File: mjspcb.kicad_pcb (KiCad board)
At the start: 2 copper layers, 83.3 x 40.1 mm, 78 parts, among them P1 Batteries, P10 Lipo, P2 serial breakout, P3 I2C breakout, P4 GPS, P5 piezo, P6 BPW34, P7 electrodes, P8 perfboard breakout, P9 reset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

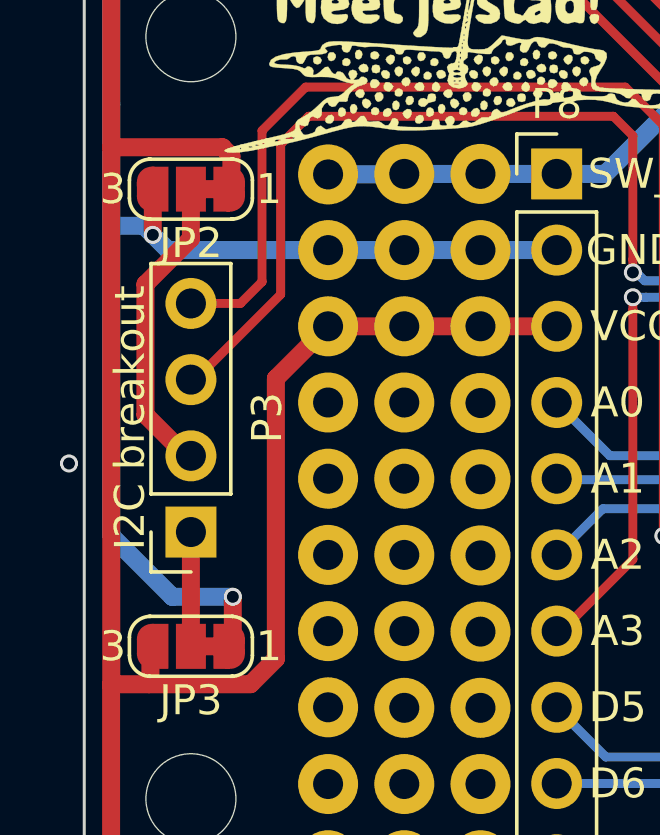
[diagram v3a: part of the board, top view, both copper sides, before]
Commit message: Fix DRC errors in solder jumper footprint
This uses a modified solder jumper footprint that has a graphic polygon
rather than overlapping pads to connect the default pins, which prevents
DRC errors. See: https://github.com/KiCad/kicad-footprints/issues/1165
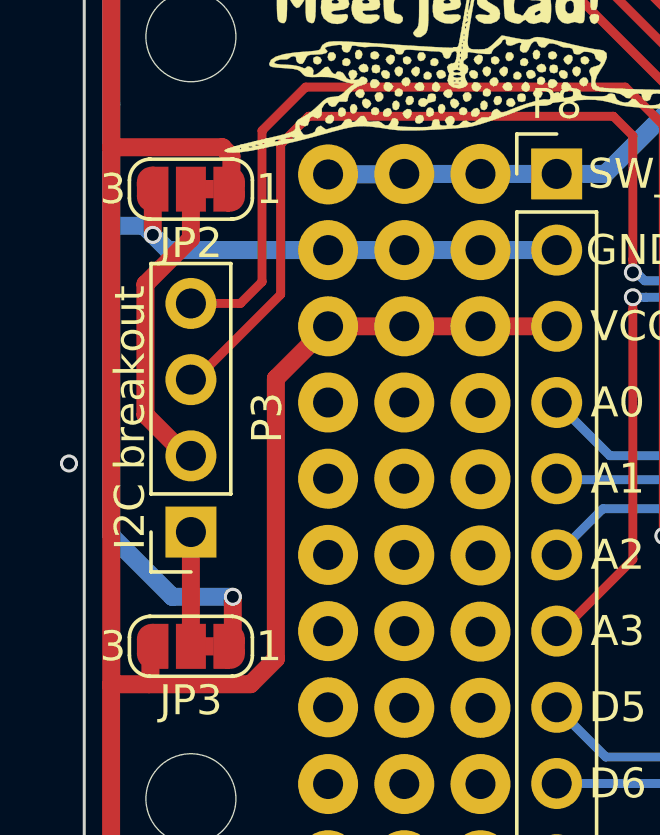
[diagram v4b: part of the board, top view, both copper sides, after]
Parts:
- JP2, JP3: footprint Jumper:SolderJumper-3_P1.3mm_Bridged12_RoundedPad1.0x1.5mm_NumberLabels -> meetjestad:SolderJumper-3_P1.3mm_Bridged12_RoundedPad1.0x1.5mm_NumberLabels
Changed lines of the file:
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@@
     (add_net VIN)
   )
-  (module Jumper:SolderJumper-3_P1.3mm_Bridged12_RoundedPad1.0x1.5mm_NumberLabels (layer F.Cu)
+  (module meetjestad:SolderJumper-3_P1.3mm_Bridged12_RoundedPad1.0x1.5mm_NumberLabels (layer F.Cu)
     (at 139.7 128.27 180)
     (descr "SMD Solder 3-pad Jumper, 1x1.5mm rounded Pads, 0.3mm gap, pads 1-2 bridged with 1 copper strip, labeled with numbers")
@@
       (effects (font (size 1 1) (thickness 0.15)))
     )
-    (fp_arc (start -1.35 -0.3) (end -1.35 -1) (angle -90) (layer F.SilkS) (width 0.12))
-    (fp_arc (start -1.35 0.3) (end -2.05 0.3) (angle -90) (layer F.SilkS) (width 0.12))
-    (fp_arc (start 1.35 0.3) (end 1.35 1) (angle -90) (layer F.SilkS) (width 0.12))
-    (fp_arc (start 1.35 -0.3) (end 2.05 -0.3) (angle -90) (layer F.SilkS) (width 0.12))
-    (fp_line (start 2.3 1.25) (end -2.3 1.25) (layer F.CrtYd) (width 0.05))
-    (fp_line (start 2.3 1.25) (end 2.3 -1.25) (layer F.CrtYd) (width 0.05))
-    (fp_line (start -2.3 -1.25) (end -2.3 1.25) (layer F.CrtYd) (width 0.05))
-    (fp_line (start -2.3 -1.25) (end 2.3 -1.25) (layer F.CrtYd) (width 0.05))
-    (fp_line (start -1.4 -1) (end 1.4 -1) (layer F.SilkS) (width 0.12))
-    (fp_line (start 2.05 -0.3) (end 2.05 0.3) (layer F.SilkS) (width 0.12))
-    (fp_line (start 1.4 1) (end -1.4 1) (layer F.SilkS) (width 0.12))
-    (fp_line (start -2.05 0.3) (end -2.05 -0.3) (layer F.SilkS) (width 0.12))
+    (fp_poly (pts (xy -0.4826 0.3048) (xy -0.4826 -0.3048) (xy -0.762 -0.3048) (xy -0.762 0.3048)) (layer F.Cu) (width 0))
+    (fp_text user 3 (at 2.6 0 180) (layer F.SilkS)
+      (effects (font (size 1 1) (thickness 0.15)))
+    )
     (fp_text user 1 (at -2.6 0 180) (layer F.SilkS)
       (effects (font (size 1 1) (thickness 0.15)))
     )
-    (fp_text user 3 (at 2.6 0 180) (layer F.SilkS)
-      (effects (font (size 1 1) (thickness 0.15)))
-    )
-    (pad 2 smd rect (at 0 0 180) (size 1 1.5) (layers F.Cu F.Mask)
-      (net 43 "Net-(JP3-Pad2)"))
+    (fp_line (start -2.05 0.3) (end -2.05 -0.3) (layer F.SilkS) (width 0.12))
+    (fp_line (start 1.4 1) (end -1.4 1) (layer F.SilkS) (width 0.12))
+    (fp_line (start 2.05 -0.3) (end 2.05 0.3) (layer F.SilkS) (width 0.12))
+    (fp_line (start -1.4 -1) (end 1.4 -1) (layer F.SilkS) (width 0.12))
+    (fp_line (start -2.3 -1.25) (end 2.3 -1.25) (layer F.CrtYd) (width 0.05))
+    (fp_line (start -2.3 -1.25) (end -2.3 1.25) (layer F.CrtYd) (width 0.05))
+    (fp_line (start 2.3 1.25) (end 2.3 -1.25) (layer F.CrtYd) (width 0.05))
+    (fp_line (start 2.3 1.25) (end -2.3 1.25) (layer F.CrtYd) (width 0.05))
+    (fp_arc (start 1.35 -0.3) (end 2.05 -0.3) (angle -90) (layer F.SilkS) (width 0.12))
+    (fp_arc (start 1.35 0.3) (end 1.35 1) (angle -90) (layer F.SilkS) (width 0.12))
+    (fp_arc (start -1.35 0.3) (end -2.05 0.3) (angle -90) (layer F.SilkS) (width 0.12))
+    (fp_arc (start -1.35 -0.3) (end -1.35 -1) (angle -90) (layer F.SilkS) (width 0.12))
+    (pad 1 smd custom (at -1.3 0 180) (size 1 0.5) (layers F.Cu F.Mask)
+      (net 3 GND) (zone_connect 0)
+      (options (clearance outline) (anchor rect))
+      (primitives
+        (gr_circle (center 0 0.25) (end 0.5 0.25) (width 0))
+        (gr_circle (center 0 -0.25) (end 0.5 -0.25) (width 0))
+        (gr_poly (pts
+           (xy 0.55 -0.75) (xy 0 -0.75) (xy 0 0.75) (xy 0.55 0.75)) (width 0))
+      ))
     (pad 3 smd custom (at 1.3 0 180) (size 1 0.5) (layers F.Cu F.Mask)
       (net 2 VCC) (zone_connect 0)
@@
            (xy -0.55 -0.75) (xy 0 -0.75) (xy 0 0.75) (xy -0.55 0.75)) (width 0))
       ))
-    (pad 1 smd custom (at -1.3 0 180) (size 1 0.5) (layers F.Cu F.Mask)
-      (net 3 GND) (zone_connect 0)
-      (options (clearance outline) (anchor rect))
-      (primitives
-        (gr_circle (center 0 0.25) (end 0.5 0.25) (width 0))
-        (gr_circle (center 0 -0.25) (end 0.5 -0.25) (width 0))
-        (gr_poly (pts
-           (xy 0.55 -0.75) (xy 0 -0.75) (xy 0 0.75) (xy 0.55 0.75)) (width 0))
-        (gr_poly (pts
-           (xy 0.4 -0.3) (xy 0.9 -0.3) (xy 0.9 0.3) (xy 0.4 0.3)) (width 0))
-      ))
+    (pad 2 smd rect (at 0 0 180) (size 1 1.5) (layers F.Cu F.Mask)
+      (net 43 "Net-(JP3-Pad2)"))
   )
-  (module Jumper:SolderJumper-3_P1.3mm_Bridged12_RoundedPad1.0x1.5mm_NumberLabels (layer F.Cu)
+  (module meetjestad:SolderJumper-3_P1.3mm_Bridged12_RoundedPad1.0x1.5mm_NumberLabels (layer F.Cu)
     (at 139.7 113.03 180)
     (descr "SMD Solder 3-pad Jumper, 1x1.5mm rounded Pads, 0.3mm gap, pads 1-2 bridged with 1 copper strip, labeled with numbers")
@@
       (effects (font (size 1 1) (thickness 0.15)))
     )
-    (fp_arc (start -1.35 -0.3) (end -1.35 -1) (angle -90) (layer F.SilkS) (width 0.12))
-    (fp_arc (start -1.35 0.3) (end -2.05 0.3) (angle -90) (layer F.SilkS) (width 0.12))
-    (fp_arc (start 1.35 0.3) (end 1.35 1) (angle -90) (layer F.SilkS) (width 0.12))
-    (fp_arc (start 1.35 -0.3) (end 2.05 -0.3) (angle -90) (layer F.SilkS) (width 0.12))
-    (fp_line (start 2.3 1.25) (end -2.3 1.25) (layer F.CrtYd) (width 0.05))
-    (fp_line (start 2.3 1.25) (end 2.3 -1.25) (layer F.CrtYd) (width 0.05))
-    (fp_line (start -2.3 -1.25) (end -2.3 1.25) (layer F.CrtYd) (width 0.05))
-    (fp_line (start -2.3 -1.25) (end 2.3 -1.25) (layer F.CrtYd) (width 0.05))
-    (fp_line (start -1.4 -1) (end 1.4 -1) (layer F.SilkS) (width 0.12))
-    (fp_line (start 2.05 -0.3) (end 2.05 0.3) (layer F.SilkS) (width 0.12))
-    (fp_line (start 1.4 1) (end -1.4 1) (layer F.SilkS) (width 0.12))
-    (fp_line (start -2.05 0.3) (end -2.05 -0.3) (layer F.SilkS) (width 0.12))
+    (fp_poly (pts (xy -0.4826 0.3048) (xy -0.4826 -0.3048) (xy -0.762 -0.3048) (xy -0.762 0.3048)) (layer F.Cu) (width 0))
+    (fp_text user 3 (at 2.6 0 180) (layer F.SilkS)
+      (effects (font (size 1 1) (thickness 0.15)))
+    )
     (fp_text user 1 (at -2.6 0 180) (layer F.SilkS)
       (effects (font (size 1 1) (thickness 0.15)))
     )
-    (fp_text user 3 (at 2.6 0 180) (layer F.SilkS)
-      (effects (font (size 1 1) (thickness 0.15)))
-    )
-    (pad 2 smd rect (at 0 0 180) (size 1 1.5) (layers F.Cu F.Mask)
-      (net 42 "Net-(JP2-Pad2)"))
+    (fp_line (start -2.05 0.3) (end -2.05 -0.3) (layer F.SilkS) (width 0.12))
+    (fp_line (start 1.4 1) (end -1.4 1) (layer F.SilkS) (width 0.12))
+    (fp_line (start 2.05 -0.3) (end 2.05 0.3) (layer F.SilkS) (width 0.12))
+    (fp_line (start -1.4 -1) (end 1.4 -1) (layer F.SilkS) (width 0.12))
+    (fp_line (start -2.3 -1.25) (end 2.3 -1.25) (layer F.CrtYd) (width 0.05))
+    (fp_line (start -2.3 -1.25) (end -2.3 1.25) (layer F.CrtYd) (width 0.05))
+    (fp_line (start 2.3 1.25) (end 2.3 -1.25) (layer F.CrtYd) (width 0.05))
+    (fp_line (start 2.3 1.25) (end -2.3 1.25) (layer F.CrtYd) (width 0.05))
+    (fp_arc (start 1.35 -0.3) (end 2.05 -0.3) (angle -90) (layer F.SilkS) (width 0.12))
+    (fp_arc (start 1.35 0.3) (end 1.35 1) (angle -90) (layer F.SilkS) (width 0.12))
+    (fp_arc (start -1.35 0.3) (end -2.05 0.3) (angle -90) (layer F.SilkS) (width 0.12))
+    (fp_arc (start -1.35 -0.3) (end -1.35 -1) (angle -90) (layer F.SilkS) (width 0.12))
+    (pad 1 smd custom (at -1.3 0 180) (size 1 0.5) (layers F.Cu F.Mask)
+      (net 2 VCC) (zone_connect 0)
+      (options (clearance outline) (anchor rect))
+      (primitives
+        (gr_circle (center 0 0.25) (end 0.5 0.25) (width 0))
+        (gr_circle (center 0 -0.25) (end 0.5 -0.25) (width 0))
+        (gr_poly (pts
+           (xy 0.55 -0.75) (xy 0 -0.75) (xy 0 0.75) (xy 0.55 0.75)) (width 0))
+      ))
     (pad 3 smd custom (at 1.3 0 180) (size 1 0.5) (layers F.Cu F.Mask)
       (net 3 GND) (zone_connect 0)
@@
            (xy -0.55 -0.75) (xy 0 -0.75) (xy 0 0.75) (xy -0.55 0.75)) (width 0))
       ))
-    (pad 1 smd custom (at -1.3 0 180) (size 1 0.5) (layers F.Cu F.Mask)
-      (net 2 VCC) (zone_connect 0)
-      (options (clearance outline) (anchor rect))
-      (primitives
-        (gr_circle (center 0 0.25) (end 0.5 0.25) (width 0))
-        (gr_circle (center 0 -0.25) (end 0.5 -0.25) (width 0))
-        (gr_poly (pts
-           (xy 0.55 -0.75) (xy 0 -0.75) (xy 0 0.75) (xy 0.55 0.75)) (width 0))
-        (gr_poly (pts
-           (xy 0.4 -0.3) (xy 0.9 -0.3) (xy 0.9 0.3) (xy 0.4 0.3)) (width 0))
-      ))
+    (pad 2 smd rect (at 0 0 180) (size 1 1.5) (layers F.Cu F.Mask)
+      (net 42 "Net-(JP2-Pad2)"))
   )
   (module meetjestad:perf (layer F.Cu)

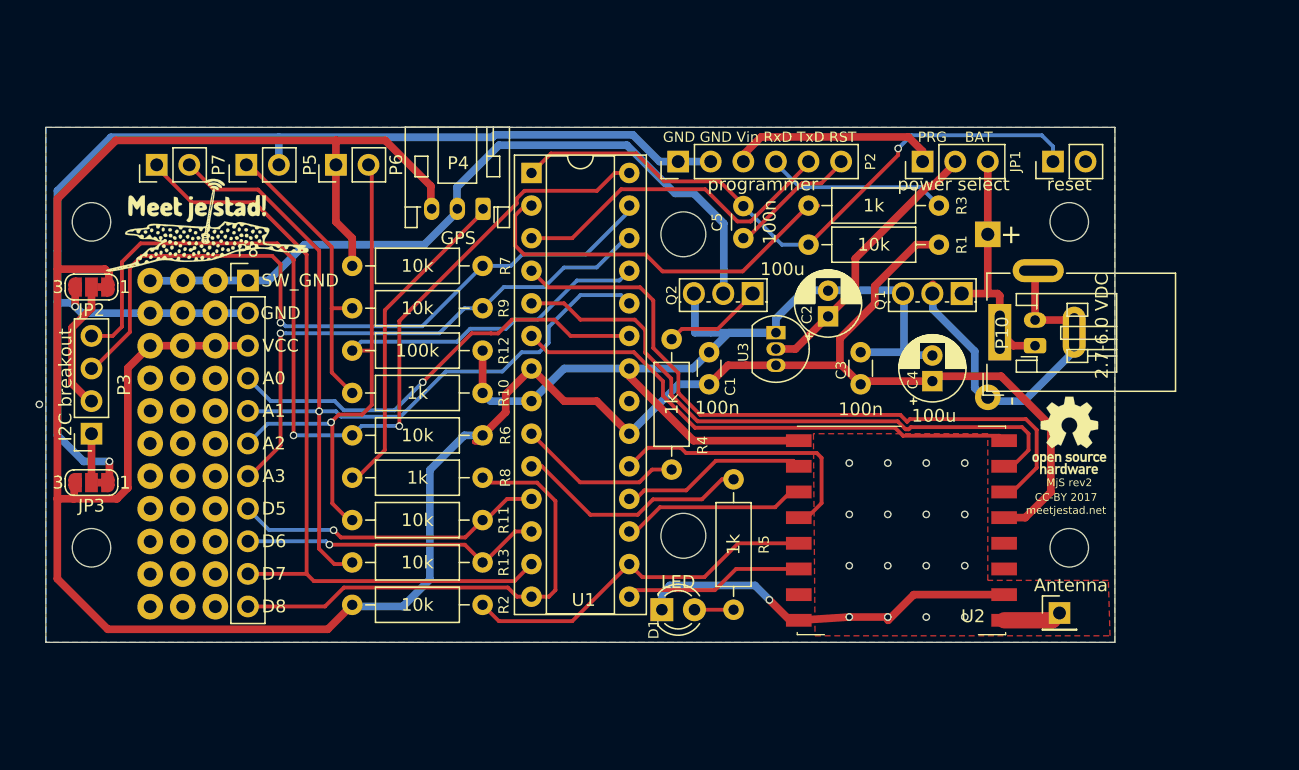
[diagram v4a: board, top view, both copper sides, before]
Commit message: Increase board size
This increases the width to 56mm, so it no longer needs extra plates to
fit into the housing. The length is also slightly increased (to make
room to mount the GPS antenna later), but kept within 100mm (which makes
prototype PCBs a lot cheaper with some suppliers).
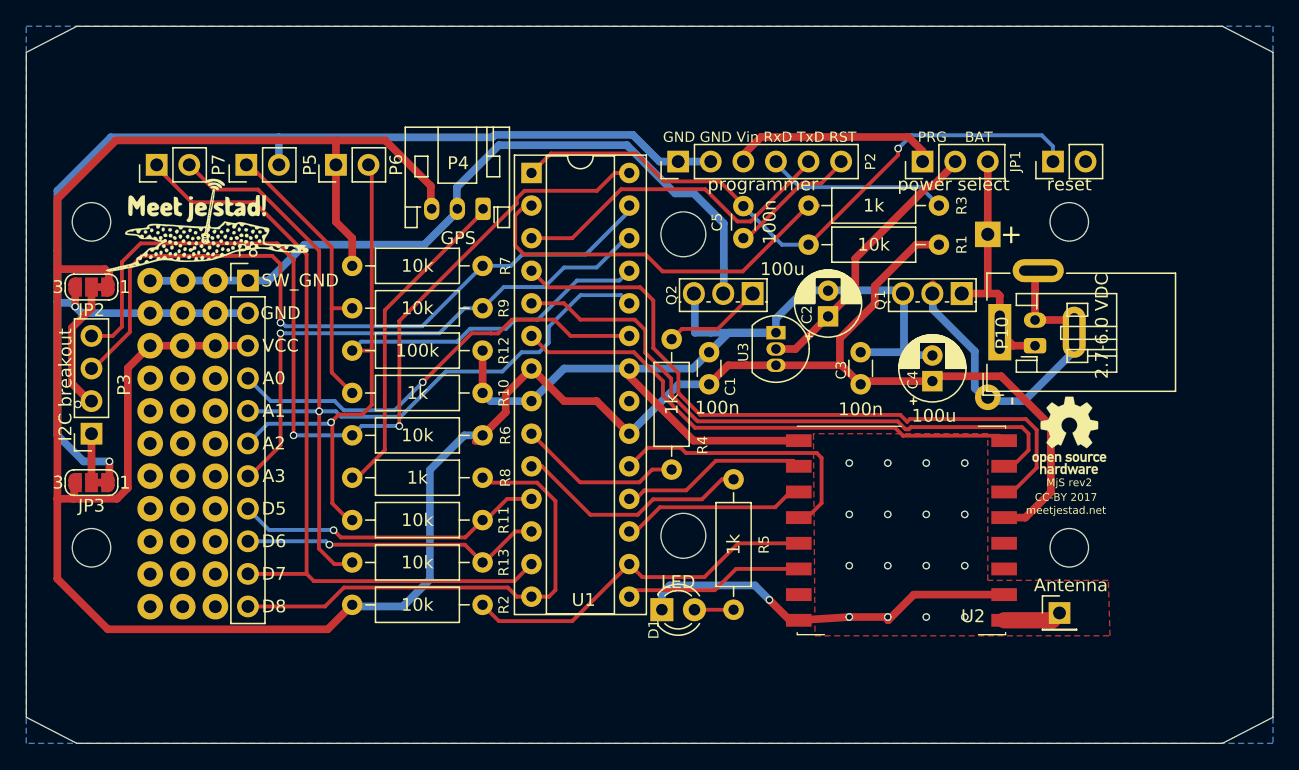
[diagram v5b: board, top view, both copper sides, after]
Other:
- board size 83.3 x 40.1 mm -> 97.2 x 55.9 mm
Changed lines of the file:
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@@
   (general
     (thickness 1.6)
-    (drawings 27)
+    (drawings 31)
     (tracks 540)
     (zones 0)
@@
     (pad_to_mask_clearance 0)
     (solder_mask_min_width 0.25)
-    (aux_axis_origin 136.144 140.716)
+    (aux_axis_origin 134.747 148.59)
+    (grid_origin 134.62 148.59)
     (visible_elements 7FFFFF7F)
     (pcbplotparams
-      (layerselection 0x010f0_80000001)
-      (usegerberextensions false)
+      (layerselection 0x010f0_ffffffff)
+      (usegerberextensions true)
       (usegerberattributes false)
       (usegerberadvancedattributes false)
       (creategerberjobfile false)
-      (excludeedgelayer false)
+      (excludeedgelayer true)
       (linewidth 0.100000)
       (plotframeref false)
       (viasonmask false)
       (mode 1)
-      (useauxorigin false)
+      (useauxorigin true)
       (hpglpennumber 1)
       (hpglpenspeed 20)
@@
       (effects (font (size 1 1) (thickness 0.15)))
     )
+    (fp_line (start 1.93 -1.25) (end 1.93 1.25) (layer F.Fab) (width 0.1))
+    (fp_line (start 1.93 1.25) (end 8.23 1.25) (layer F.Fab) (width 0.1))
+    (fp_line (start 8.23 1.25) (end 8.23 -1.25) (layer F.Fab) (width 0.1))
+    (fp_line (start 8.23 -1.25) (end 1.93 -1.25) (layer F.Fab) (width 0.1))
+    (fp_line (start 0 0) (end 1.93 0) (layer F.Fab) (width 0.1))
+    (fp_line (start 10.16 0) (end 8.23 0) (layer F.Fab) (width 0.1))
+    (fp_line (start 1.81 -1.37) (end 1.81 1.37) (layer F.SilkS) (width 0.12))
+    (fp_line (start 1.81 1.37) (end 8.35 1.37) (layer F.SilkS) (width 0.12))
+    (fp_line (start 8.35 1.37) (end 8.35 -1.37) (layer F.SilkS) (width 0.12))
+    (fp_line (start 8.35 -1.37) (end 1.81 -1.37) (layer F.SilkS) (width 0.12))
+    (fp_line (start 1.04 0) (end 1.81 0) (layer F.SilkS) (width 0.12))
+    (fp_line (start 9.12 0) (end 8.35 0) (layer F.SilkS) (width 0.12))
+    (fp_line (start -1.05 -1.5) (end -1.05 1.5) (layer F.CrtYd) (width 0.05))
+    (fp_line (start -1.05 1.5) (end 11.21 1.5) (layer F.CrtYd) (width 0.05))
+    (fp_line (start 11.21 1.5) (end 11.21 -1.5) (layer F.CrtYd) (width 0.05))
+    (fp_line (start 11.21 -1.5) (end -1.05 -1.5) (layer F.CrtYd) (width 0.05))
     (fp_text user %R (at 5.08 0 180) (layer F.Fab)
       (effects (font (size 0.8 0.8) (thickness 0.1)))
     )
-    (fp_line (start 11.21 -1.5) (end -1.05 -1.5) (layer F.CrtYd) (width 0.05))
-    (fp_line (start 11.21 1.5) (end 11.21 -1.5) (layer F.CrtYd) (width 0.05))
-    (fp_line (start -1.05 1.5) (end 11.21 1.5) (layer F.CrtYd) (width 0.05))
-    (fp_line (start -1.05 -1.5) (end -1.05 1.5) (layer F.CrtYd) (width 0.05))
-    (fp_line (start 9.12 0) (end 8.35 0) (layer F.SilkS) (width 0.12))
-    (fp_line (start 1.04 0) (end 1.81 0) (layer F.SilkS) (width 0.12))
-    (fp_line (start 8.35 -1.37) (end 1.81 -1.37) (layer F.SilkS) (width 0.12))
-    (fp_line (start 8.35 1.37) (end 8.35 -1.37) (layer F.SilkS) (width 0.12))
-    (fp_line (start 1.81 1.37) (end 8.35 1.37) (layer F.SilkS) (width 0.12))
-    (fp_line (start 1.81 -1.37) (end 1.81 1.37) (layer F.SilkS) (width 0.12))
-    (fp_line (start 10.16 0) (end 8.23 0) (layer F.Fab) (width 0.1))
-    (fp_line (start 0 0) (end 1.93 0) (layer F.Fab) (width 0.1))
-    (fp_line (start 8.23 -1.25) (end 1.93 -1.25) (layer F.Fab) (width 0.1))
-    (fp_line (start 8.23 1.25) (end 8.23 -1.25) (layer F.Fab) (width 0.1))
-    (fp_line (start 1.93 1.25) (end 8.23 1.25) (layer F.Fab) (width 0.1))
-    (fp_line (start 1.93 -1.25) (end 1.93 1.25) (layer F.Fab) (width 0.1))
-    (pad 2 thru_hole oval (at 10.16 0 180) (size 1.6 1.6) (drill 0.8) (layers *.Cu *.Mask)
-      (net 5 RST))
     (pad 1 thru_hole circle (at 0 0 180) (size 1.6 1.6) (drill 0.8) (layers *.Cu *.Mask)
       (net 2 VCC))
+    (pad 2 thru_hole oval (at 10.16 0 180) (size 1.6 1.6) (drill 0.8) (layers *.Cu *.Mask)
+      (net 5 RST))
     (model ${KISYS3DMOD}/Resistor_THT.3dshapes/R_Axial_DIN0207_L6.3mm_D2.5mm_P10.16mm_Horizontal.wrl
       (at (xyz 0 0 0))
@@
     )
   )
+  (gr_line (start 138.557 148.59) (end 134.62 146.558) (layer Edge.Cuts) (width 0.1))
+  (gr_line (start 138.557 92.71) (end 134.62 94.742) (layer Edge.Cuts) (width 0.1))
+  (gr_line (start 231.775 94.742) (end 227.838 92.71) (layer Edge.Cuts) (width 0.1))
+  (gr_line (start 231.775 146.558) (end 227.838 148.59) (layer Edge.Cuts) (width 0.1))
   (gr_text "GND GND Vin RxD TxD RST" (at 191.77 101.346) (layer F.SilkS)
     (effects (font (size 0.8 0.8) (thickness 0.1)))
@@
     (effects (font (size 1 1) (thickness 0.15)) (justify mirror))
   )
-  (gr_line (start 219.456 140.716) (end 136.144 140.716) (layer Edge.Cuts) (width 0.1))
-  (gr_line (start 219.456 100.584) (end 219.456 140.716) (layer Edge.Cuts) (width 0.1))
-  (gr_line (start 136.144 100.584) (end 219.456 100.584) (layer Edge.Cuts) (width 0.1))
-  (gr_line (start 136.144 140.716) (end 136.144 100.584) (layer Edge.Cuts) (width 0.1))
+  (gr_line (start 227.838 148.59) (end 138.557 148.59) (layer Edge.Cuts) (width 0.1))
+  (gr_line (start 231.775 94.742) (end 231.775 146.558) (layer Edge.Cuts) (width 0.1))
+  (gr_line (start 138.557 92.71) (end 227.838 92.71) (layer Edge.Cuts) (width 0.1))
+  (gr_line (start 134.62 146.558) (end 134.62 94.742) (layer Edge.Cuts) (width 0.1))
   (gr_text programmer (at 192.024 105.029) (layer F.SilkS)
     (effects (font (size 1 1) (thickness 0.1)))
@@
     (effects (font (size 1.5 1.5) (thickness 0.3)))
   )
-  (via (at 135.636 122.174) (size 0.6) (drill 0.4) (layers F.Cu B.Cu) (net 0))
+  (via (at 138.636 122.174) (size 0.6) (drill 0.4) (layers F.Cu B.Cu) (net 0))
   (segment (start 215.138 138.43) (end 214.568 139) (width 1.27) (layer F.Cu) (net 1) (status 30))
   (segment (start 214.568 139) (end 210.82 139) (width 1.27) (layer F.Cu) (net 1) (status 30))
@@
     (polygon
       (pts
-        (xy 136.144 100.584) (xy 219.456 100.584) (xy 219.456 140.716) (xy 136.144 140.716)
+        (xy 134.62 92.71) (xy 231.775 92.71) (xy 231.775 148.59) (xy 134.62 148.59)
       )
     )
